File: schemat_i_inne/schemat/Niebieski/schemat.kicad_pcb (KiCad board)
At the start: 2 copper layers, 260.4 x 151.1 mm, 23 parts, among them J1 Hole1, J2 Hole2, J3 Hole3, J4 Hole4, J5 RJ45, SW1 SW_DIP_x01, SW2 Left, SW3 Up, SW4 Down, SW5 Right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

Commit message: Koncowe sciezki i adapter
Ukonczono poprawianie sciezek i poprawnie zrobiono adapter
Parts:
- moved BT1 3.64 mm to (188.5, 63.0), turned to 180 degrees
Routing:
- net GND: track 766.1 -> 858.1 mm
- net VCC: track 285.4 -> 357.9 mm
- net Net-(J5-Pad4): track 106.3 -> 131.7 mm
- net Net-(J5-Pad5): track 113.7 -> 122.6 mm
- net Net-(RV1-Pad2): track 59.2 -> 65.2 mm
- net Net-(BT1-Pad1): track 7.67 -> 2.92 mm
- net Net-(J5-Pad7): track 142.1 -> 146.5 mm
- net Net-(U1-Pad23): track 54.1 -> 50.2 mm
- net Net-(RV1-Pad1): track 25.2 -> 28.2 mm
- net Net-(J5-Pad6): track 132.4 -> 133.7 mm
- net Net-(U1-Pad26): track 50.0 -> 51.0 mm
- net Net-(U1-Pad24): track 51.5 -> 50.8 mm
- net Net-(U1-Pad25): track 50.3 -> 50.9 mm

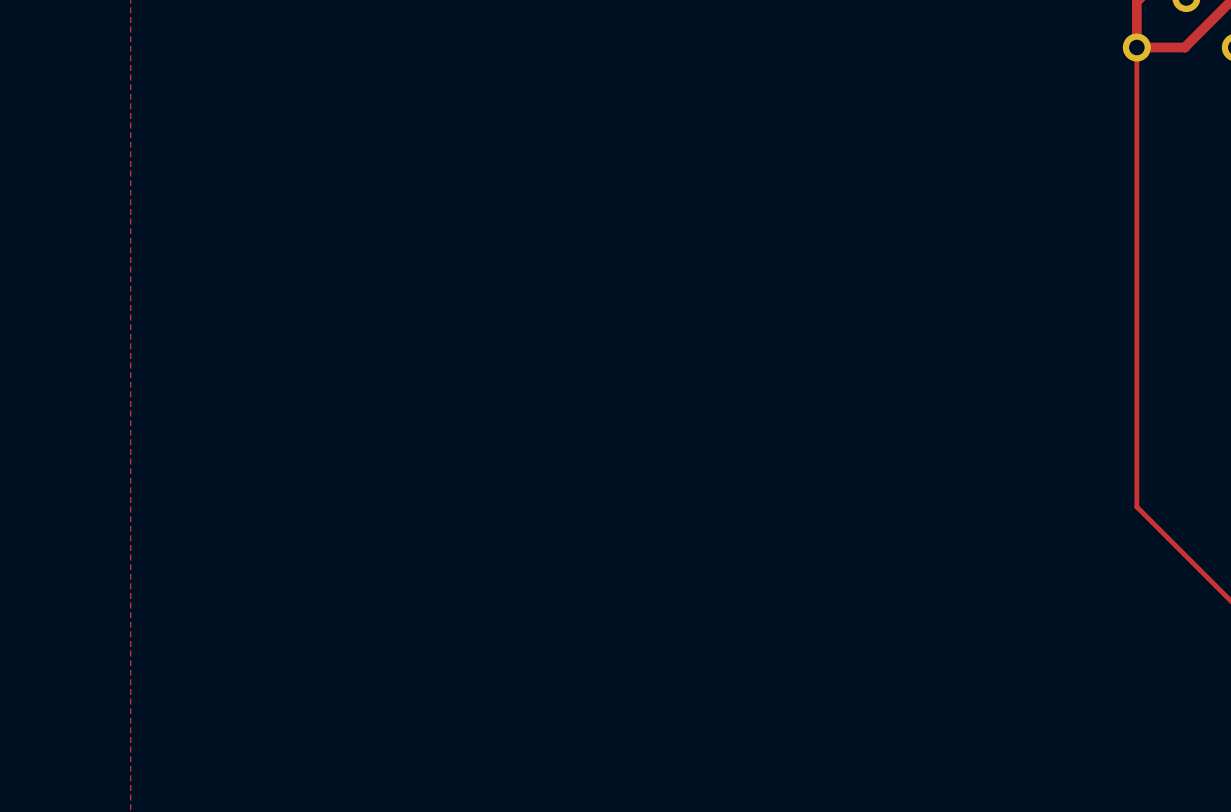
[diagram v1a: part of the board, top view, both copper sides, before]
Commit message: Logo i wymiary
Dodano "by KK" i wymiary plyty glownej
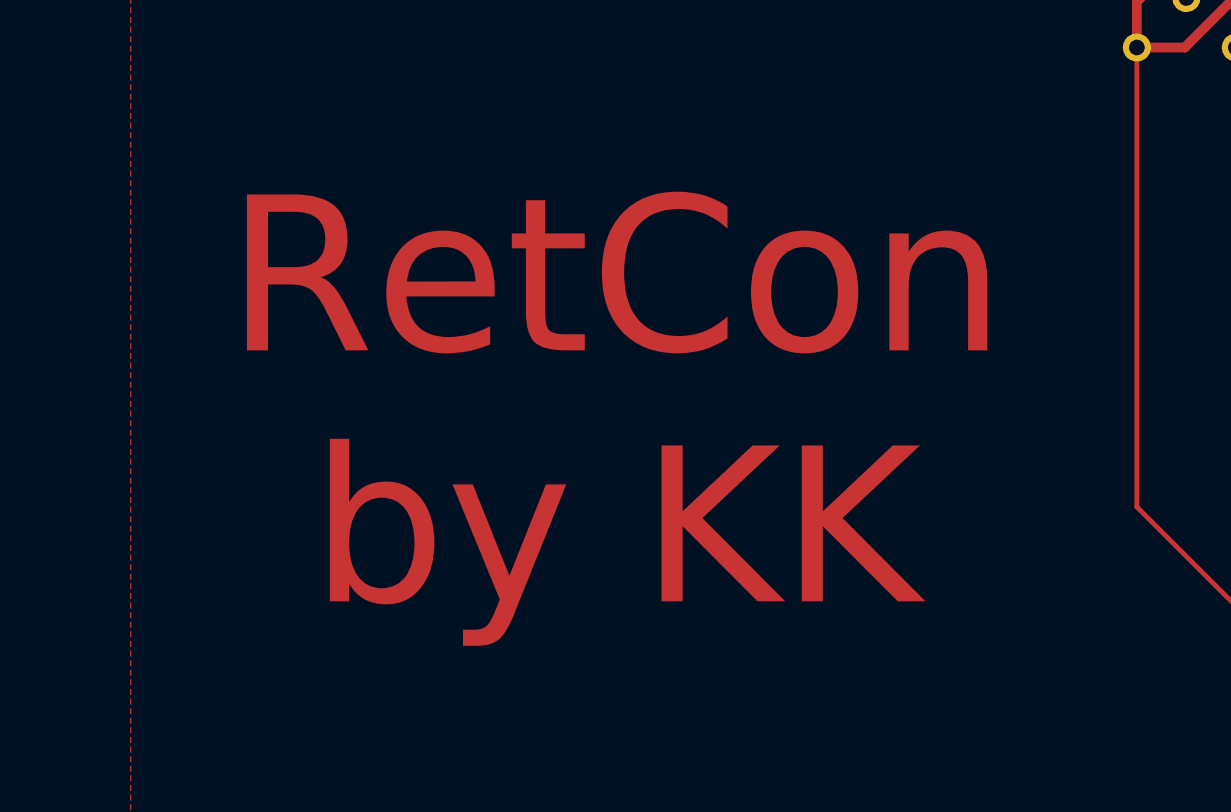
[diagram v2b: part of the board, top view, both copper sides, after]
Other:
- board text added: "RetCon by KK"
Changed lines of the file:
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@@
   (general
     (thickness 1.6)
-    (drawings 4)
+    (drawings 7)
     (tracks 353)
     (zones 0)
@@
     )
   )
+  (gr_text "RetCon\nby KK" (at 70.612 80.772) (layer F.Cu)
+    (effects (font (size 8 8) (thickness 1)))
+  )
+  (dimension 90.424 (width 0.12) (layer F.SilkS)
+    (gr_text "90,424 mm" (at 244.094 98.552 270) (layer F.SilkS)
+      (effects (font (size 1 1) (thickness 0.15)))
+    )
+    (feature1 (pts (xy 238.76 143.764) (xy 243.410421 143.764)))
+    (feature2 (pts (xy 238.76 53.34) (xy 243.410421 53.34)))
+    (crossbar (pts (xy 242.824 53.34) (xy 242.824 143.764)))
+    (arrow1a (pts (xy 242.824 143.764) (xy 242.237579 142.637496)))
+    (arrow1b (pts (xy 242.824 143.764) (xy 243.410421 142.637496)))
+    (arrow2a (pts (xy 242.824 53.34) (xy 242.237579 54.466504)))
+    (arrow2b (pts (xy 242.824 53.34) (xy 243.410421 54.466504)))
+  )
+  (dimension 193.04 (width 0.12) (layer F.SilkS)
+    (gr_text "193,040 mm" (at 142.24 48.514) (layer F.SilkS)
+      (effects (font (size 1 1) (thickness 0.15)))
+    )
+    (feature1 (pts (xy 238.76 53.34) (xy 238.76 49.197579)))
+    (feature2 (pts (xy 45.72 53.34) (xy 45.72 49.197579)))
+    (crossbar (pts (xy 45.72 49.784) (xy 238.76 49.784)))
+    (arrow1a (pts (xy 238.76 49.784) (xy 237.633496 50.370421)))
+    (arrow1b (pts (xy 238.76 49.784) (xy 237.633496 49.197579)))
+    (arrow2a (pts (xy 45.72 49.784) (xy 46.846504 50.370421)))
+    (arrow2b (pts (xy 45.72 49.784) (xy 46.846504 49.197579)))
+  )
   (gr_line (start 276.86 15.24) (end 16.51 15.24) (layer Edge.Cuts) (width 0.05))
